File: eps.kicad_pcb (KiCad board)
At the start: 4 copper layers, 95.9 x 90.2 mm, 184 parts, among them J1 PC104-8BIT, J2 PC104PTH, J3 PC104PTH, J4 PC104PTH, J5 PC104PTH, P1 3pin-DC-power, P2 3pin-DC-power, Q10 CSD17551Q3A, Q11 CSD17551Q3A, Q12 CSD17551Q3A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

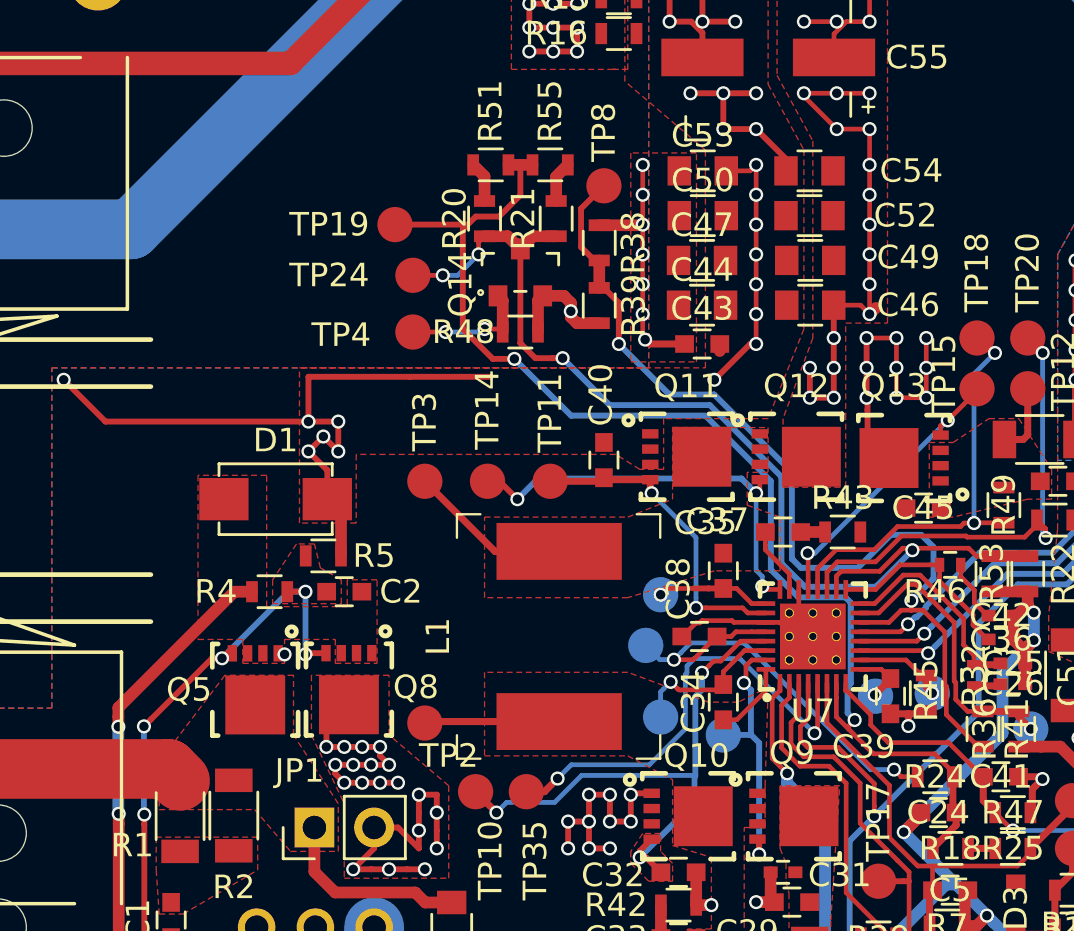
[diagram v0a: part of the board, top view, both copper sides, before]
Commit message: Fixed #8 and Fixed #14 officially and put correct footprints into layout. Needs to be fixed (specifically VSYS pin of the BMS needs to be connected)
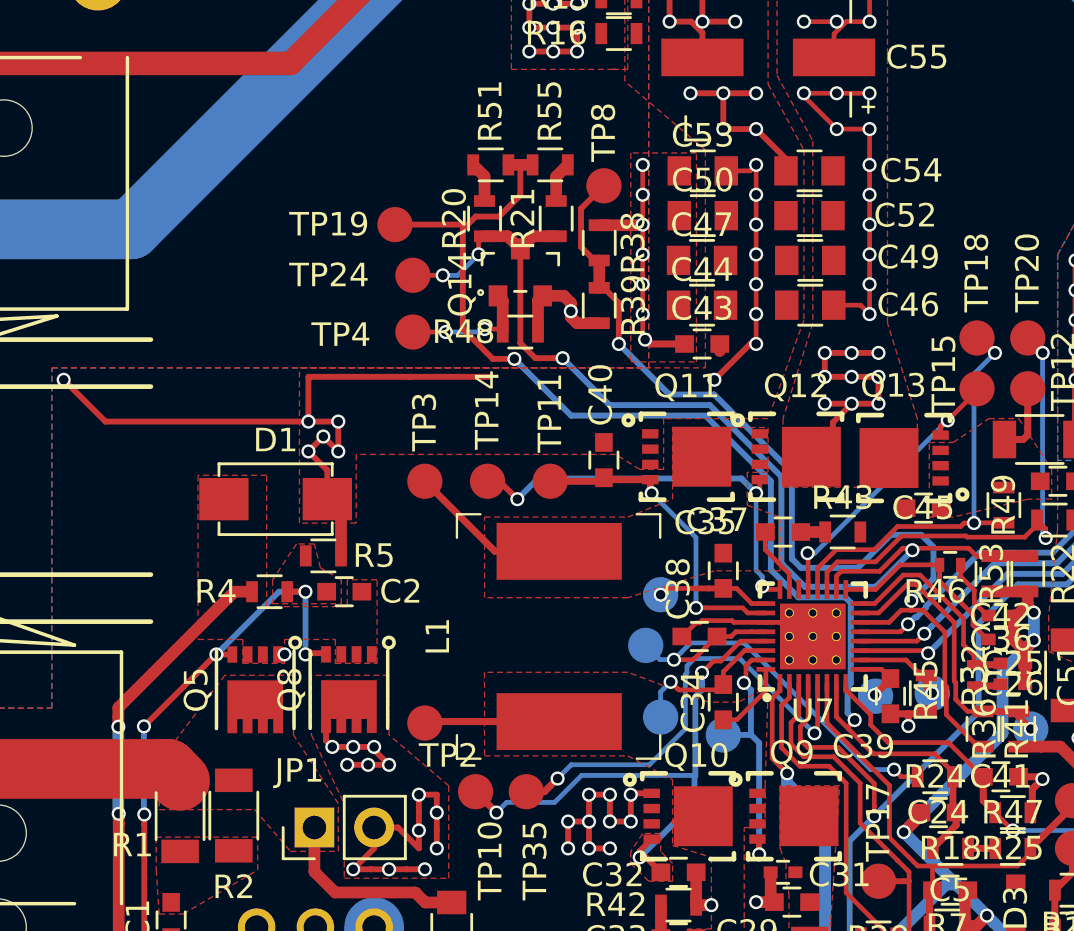
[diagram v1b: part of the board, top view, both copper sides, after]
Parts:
- Q5, Q8: footprint SFUSat:8-PowerWDFN -> SFUSat:POWERDI3333-8
- turned Q5 to 180 degrees
- turned Q8 to 180 degrees
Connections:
- Q10 pad 9: (no net) -> Net-(C33-Pad1)
- Q11 pad 9: (no net) -> Net-(C35-Pad1)
- Q12 pad 9: (no net) -> /VSYS_UP
- Q13 pad 5: GNDPWR -> /VSYS_UP
- Q13 pad 6: GNDPWR -> /VSYS_UP
- Q13 pad 7: GNDPWR -> /VSYS_UP
- Q13 pad 8: GNDPWR -> /VSYS_UP
- Q13 pad 9: (no net) -> /VSYS_UP
- Q5 pad 9: (no net) -> /BMS/VIN+
- Q8 pad 9: (no net) -> Net-(C17-Pad1)
- Q9 pad 9: (no net) -> Net-(C29-Pad1)
- U7 pad 22: GNDPWR -> /VSYS_UP
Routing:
- net GNDPWR: track 160.4 -> 146.1 mm, vias 80 -> 71
- net /VSYS_UP: track 47.4 -> 51.5 mm, vias 32 -> 36
- net Net-(C17-Pad1): track 56.0 -> 52.0 mm, vias 38 -> 32
- net Net-(C2-Pad1): track 23.9 -> 23.7 mm, vias 3 -> 2
- net (no net): track 0.00 -> 0.15 mm, vias 0 -> 1

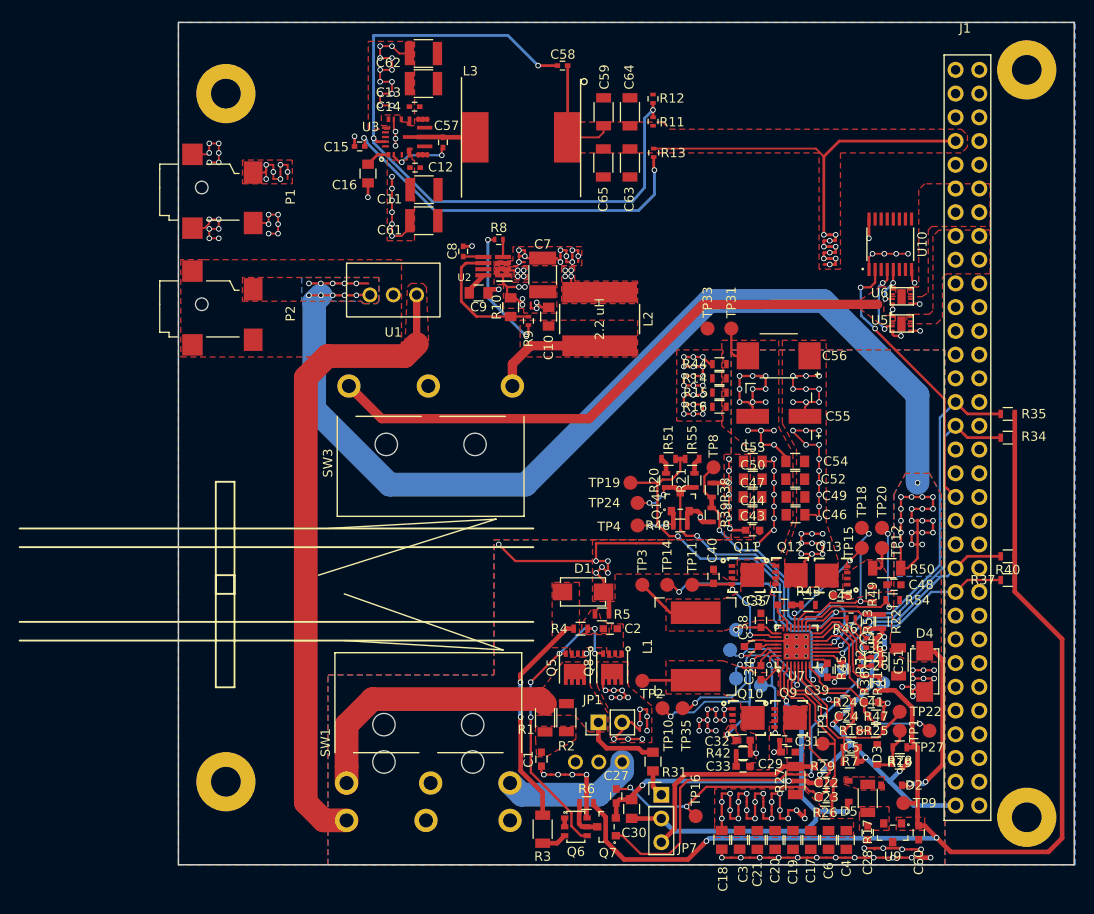
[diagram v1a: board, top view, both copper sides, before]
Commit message: imporved polygons, connected DPL_EN
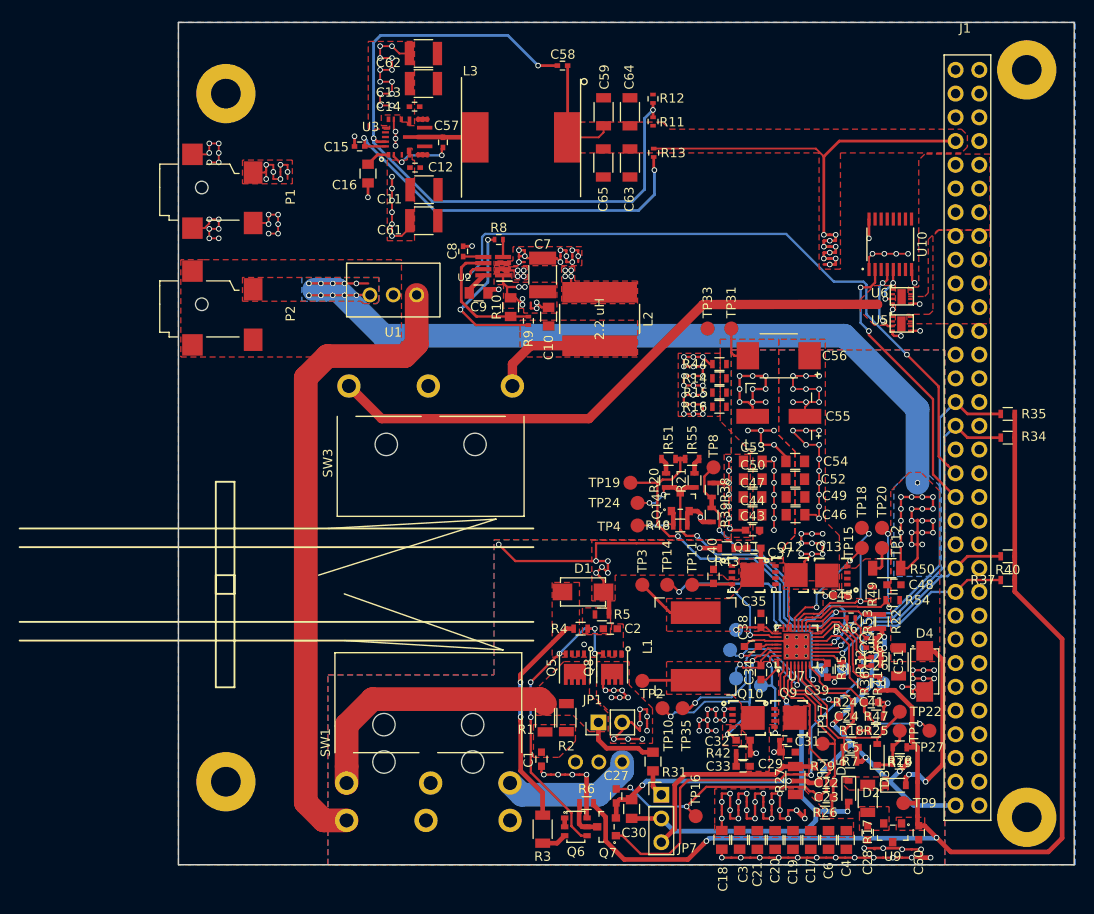
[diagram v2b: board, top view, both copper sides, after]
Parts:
- moved R43 10.6 mm to (163.7, 101.1), turned to 180 degrees
- moved C37 6.92 mm to (166.6, 101.1), turned to 180 degrees
- moved D2 0.42 mm to (181.8, 126.5)
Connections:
- U2 pad 7: /1.6A_Regulator_PDB/Deploy.EN -> /DPL_EN
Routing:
- net /DPL_EN: track 0.00 -> 74.6 mm, vias 0 -> 2
- net /pack+: track 164.6 -> 140.9 mm
- net /1.6A_Regulator_PDB/1.6A: track 26.6 -> 29.9 mm
- net Net-(C15-Pad1): track 40.1 -> 42.4 mm
- net Net-(C35-Pad1): track 11.3 -> 10.3 mm
- net GNDPWR: track 146.1 -> 147.0 mm, vias 71 -> 72
- net /BMS/ILIM_HIZ: track 20.0 -> 20.7 mm
- net Net-(U10-Pad4): track 8.06 -> 7.37 mm
- net Net-(Q13-Pad4): track 12.5 -> 13.0 mm
- removed copper zone on F.Cu, net /return

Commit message: added pull down on deployment enable pin incase the OBC output is undefined
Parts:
- added R23: 1K, SFUSat-res:R_0402, F.Cu at (139.3, 66.5)
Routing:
- net /DPL_EN: track 74.6 -> 76.5 mm, vias 2 -> 3
- net GND: track 150.6 -> 151.7 mm, vias 67 -> 68
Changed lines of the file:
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@@
 (kicad_pcb (version 4) (host pcbnew 4.0.7-e2-6376~58~ubuntu16.04.1)
   (general
-    (links 488)
-    (no_connects 75)
+    (links 490)
+    (no_connects 74)
     (area 104.924999 44.754999 200.965001 135.075001)
     (thickness 1.6)
     (drawings 48)
-    (tracks 1673)
+    (tracks 1680)
     (zones 0)
-    (modules 184)
+    (modules 185)
     (nets 141)
   )
@@
   (layers
     (0 F.Cu signal)
-    (1 GND.Cu power hide)
+    (1 GND.Cu power)
     (2 PWR.Cu power)
     (31 B.Cu signal)
-    (33 F.Adhes user hide)
+    (33 F.Adhes user)
     (35 F.Paste user)
     (36 B.SilkS user)
-    (37 F.SilkS user hide)
+    (37 F.SilkS user)
     (38 B.Mask user)
     (39 F.Mask user)
@@
     (44 Edge.Cuts user)
     (45 Margin user hide)
-    (47 F.CrtYd user hide)
+    (47 F.CrtYd user)
     (49 F.Fab user hide)
   )
@@
       (net 80 /BMS/ILIM_HIZ))
   )
+  (module SFUSat-res:R_0402 (layer F.Cu)
+    (at 139.29 66.547)
+    (descr "Resistor SMD 0402, reflow soldering, Vishay (see dcrcw.pdf)")
+    (tags "resistor 0402")
+    (attr smd)
+    (fp_text reference R23 (at 0 -1.35) (layer F.SilkS)
+      (effects (font (size 1 1) (thickness 0.15)))
+    )
+    (fp_text value 1K (at 0 1.45) (layer F.Fab)
+      (effects (font (size 1 1) (thickness 0.15)))
+    )
+    (fp_text user %R (at 0 -1.35) (layer F.Fab)
+      (effects (font (size 1 1) (thickness 0.15)))
+    )
+    (fp_line (start -0.5 0.25) (end -0.5 -0.25) (layer F.Fab) (width 0.1))
+    (fp_line (start 0.5 0.25) (end -0.5 0.25) (layer F.Fab) (width 0.1))
+    (fp_line (start 0.5 -0.25) (end 0.5 0.25) (layer F.Fab) (width 0.1))
+    (fp_line (start -0.5 -0.25) (end 0.5 -0.25) (layer F.Fab) (width 0.1))
+    (fp_line (start 0.25 -0.53) (end -0.25 -0.53) (layer F.SilkS) (width 0.12))
+    (fp_line (start -0.25 0.53) (end 0.25 0.53) (layer F.SilkS) (width 0.12))
+    (fp_line (start -0.8 -0.45) (end 0.8 -0.45) (layer F.CrtYd) (width 0.05))
+    (fp_line (start -0.8 -0.45) (end -0.8 0.45) (layer F.CrtYd) (width 0.05))
+    (fp_line (start 0.8 0.45) (end 0.8 -0.45) (layer F.CrtYd) (width 0.05))
+    (fp_line (start 0.8 0.45) (end -0.8 0.45) (layer F.CrtYd) (width 0.05))
+    (pad 1 smd rect (at -0.45 0) (size 0.4 0.6) (layers F.Cu F.Paste F.Mask)
+      (net 109 /DPL_EN) (solder_paste_margin -0.02))
+    (pad 2 smd rect (at 0.45 0) (size 0.4 0.6) (layers F.Cu F.Paste F.Mask)
+      (net 42 GND) (solder_paste_margin -0.02))
+    (model Resistors_SMD.3dshapes/R_0402.wrl
+      (at (xyz 0 0 0))
+      (scale (xyz 1 1 1))
+      (rotate (xyz 0 0 0))
+    )
+  )
   (gr_line (start 162.912 79.882) (end 162.912 87.502) (layer F.Mask) (width 1))
   (gr_text "Double check trace widths for current" (at 62.074 107.822) (layer F.CrtYd)
@@
   (gr_line (start 200.89 135) (end 200.89 44.83) (layer Edge.Cuts) (width 0.15))
   (via (at 148.429304 111.413922) (size 0.6) (drill 0.4) (layers F.Cu B.Cu) (net 0))
+  (segment (start 139.74 66.547) (end 140.814 66.547) (width 0.25) (layer F.Cu) (net 42))
+  (via (at 140.814 66.547) (size 0.6) (drill 0.4) (layers F.Cu B.Cu) (net 42))
   (segment (start 136.010985 68.767765) (end 136.435249 68.767765) (width 0.25) (layer F.Cu) (net 42))
   (segment (start 135.884235 68.767765) (end 136.010985 68.767765) (width 0.25) (layer F.Cu) (net 42))
@@
   (segment (start 172.592 85.47) (end 173.58 85.47) (width 0.2) (layer F.Cu) (net 104))
   (via (at 173.58 85.47) (size 0.6) (drill 0.4) (layers F.Cu B.Cu) (net 104))
+  (segment (start 155.8762 58.33476) (end 160.499 58.33476) (width 0.2) (layer F.Cu) (net 105))
+  (segment (start 160.499 58.33476) (end 173.24176 58.33476) (width 0.2) (layer F.Cu) (net 105))
   (segment (start 146.65046 57.13376) (end 149.97614 57.13376) (width 0.2) (layer F.Cu) (net 105))
   (segment (start 149.97614 57.13376) (end 150.51172 56.59818) (width 0.2) (layer F.Cu) (net 105))
   (segment (start 150.51172 56.59818) (end 150.51172 55.89818) (width 0.2) (layer F.Cu) (net 105))
-  (segment (start 155.8762 58.33476) (end 173.24176 58.33476) (width 0.2) (layer F.Cu) (net 105))
   (segment (start 173.24176 58.33476) (end 174.088 59.181) (width 0.2) (layer F.Cu) (net 105))
   (segment (start 174.723 70.738) (end 174.088 70.738) (width 0.3) (layer F.Cu) (net 105))
@@
   (segment (start 188.19 88.01) (end 189.46 89.28) (width 0.3) (layer F.Cu) (net 108))
   (segment (start 189.46 89.28) (end 193.023 89.28) (width 0.3) (layer F.Cu) (net 108))
+  (segment (start 137.893 66.547) (end 138.84 66.547) (width 0.25) (layer F.Cu) (net 109))
+  (segment (start 137.827201 67.470055) (end 137.827201 66.612799) (width 0.25) (layer B.Cu) (net 109))
+  (segment (start 137.827201 66.612799) (end 137.893 66.547) (width 0.25) (layer B.Cu) (net 109))
+  (via (at 137.893 66.547) (size 0.6) (drill 0.4) (layers F.Cu B.Cu) (net 109))
   (segment (start 135.988 72.008) (end 136.287999 71.708001) (width 0.25) (layer F.Cu) (net 109))
   (segment (start 136.287999 71.708001) (end 136.287999 71.483501) (width 0.25) (layer F.Cu) (net 109))

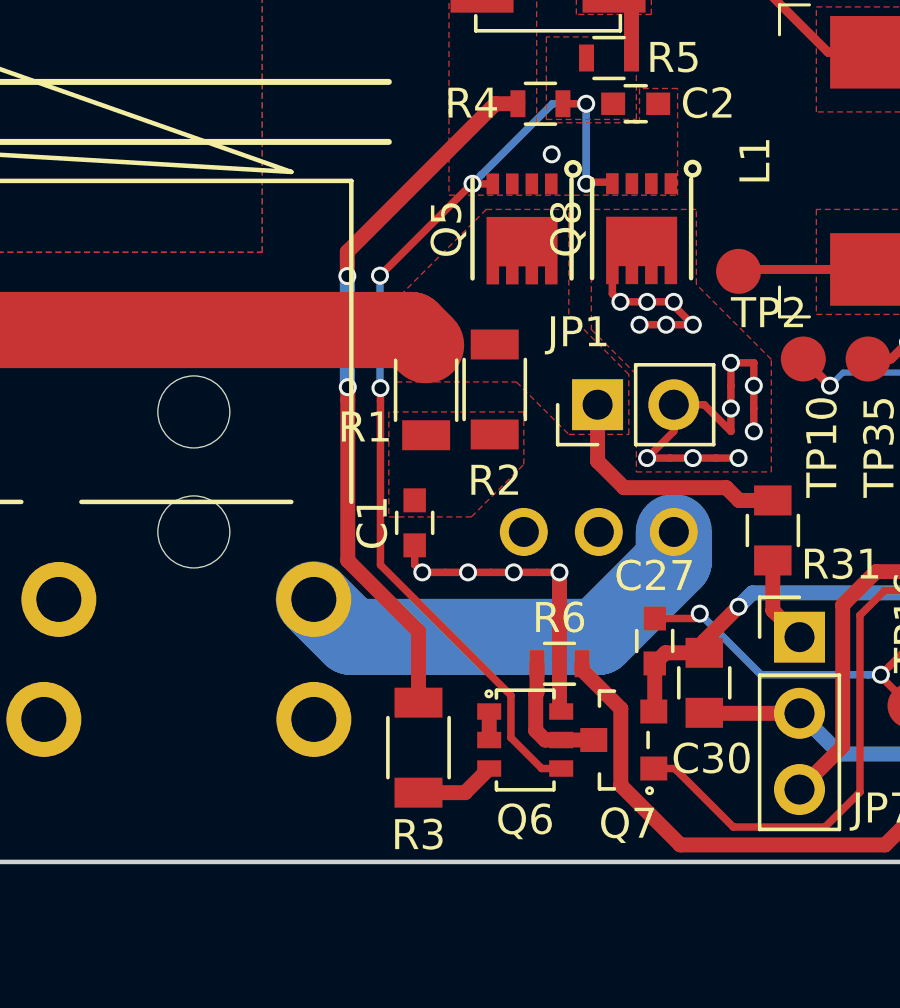
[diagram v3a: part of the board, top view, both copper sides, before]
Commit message: Fix Q6 footprint and redo traces
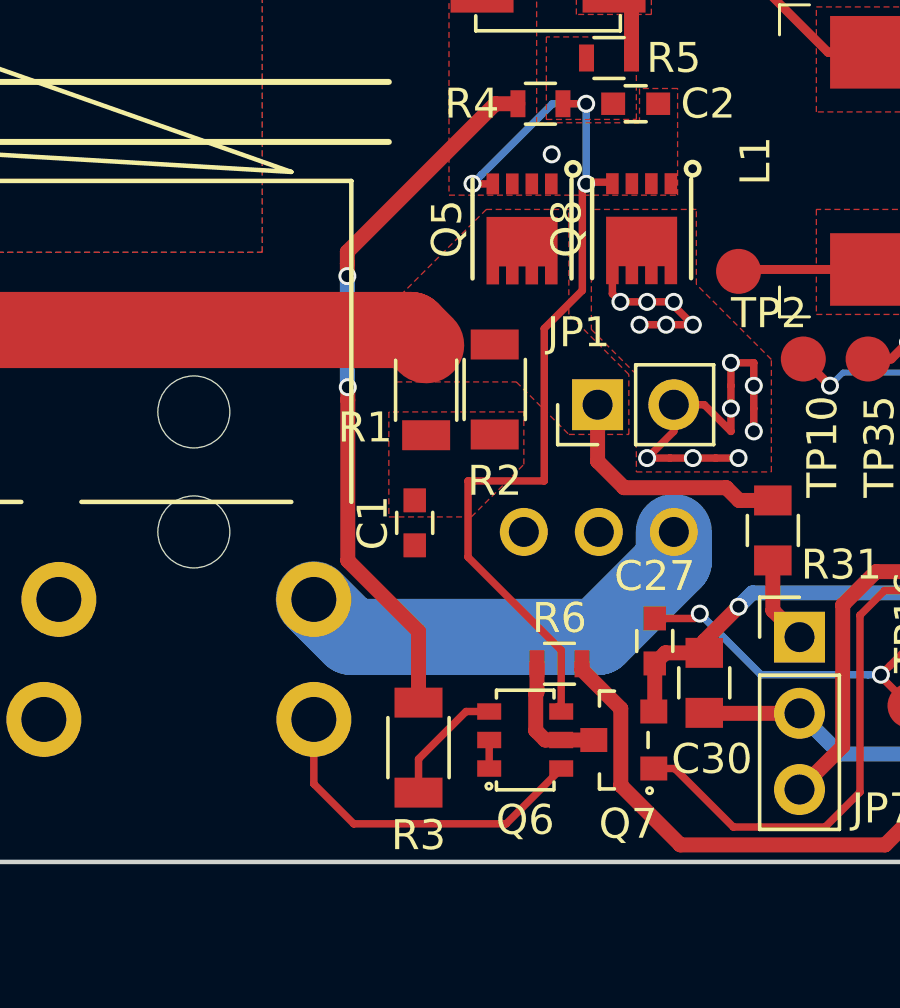
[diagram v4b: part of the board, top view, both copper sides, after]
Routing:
- net GNDPWR: track 147.0 -> 150.3 mm, vias 72 -> 68
- net Net-(C2-Pad2): track 33.7 -> 32.1 mm, vias 5 -> 3
- net Net-(Q6-Pad3): track 2.69 -> 4.13 mm

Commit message: Fixed Q6 routing
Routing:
- net Net-(C2-Pad2): track 32.1 -> 33.6 mm, vias 3 -> 5
- net GNDPWR: track 150.3 -> 151.5 mm, vias 68 -> 70
